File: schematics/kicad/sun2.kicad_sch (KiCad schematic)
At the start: 0 parts

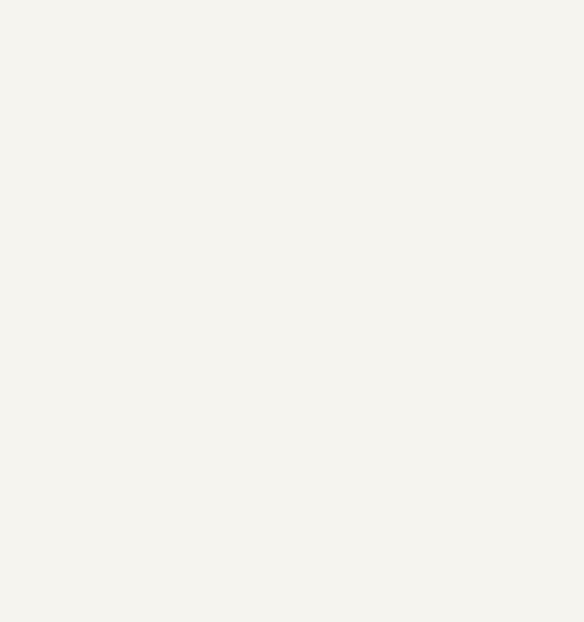
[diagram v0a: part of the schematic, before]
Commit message: System clock generator
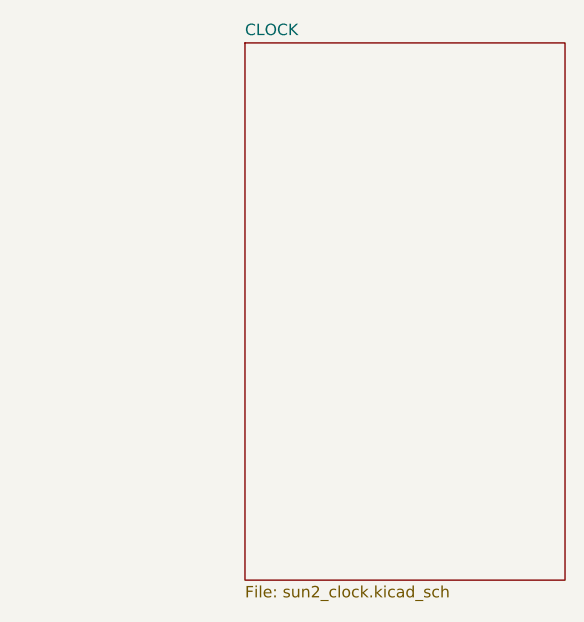
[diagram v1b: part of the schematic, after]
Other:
- added sheet CLOCK (sun2_clock.kicad_sch)
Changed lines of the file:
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@@
+		)
+	)
+	(sheet
+		(at 100.33 35.56)
+		(size 35.56 59.69)
+		(exclude_from_sim no)
+		(in_bom yes)
+		(on_board yes)
+		(dnp no)
+		(fields_autoplaced yes)
+		(stroke
+			(width 0.1524)
+			(type solid)
+		)
+		(fill
+			(color 0 0 0 0.0000)
+		)
+		(property "Sheetname" "CLOCK"
+			(at 100.33 34.8484 0)
+			(effects
+				(font
+					(size 1.27 1.27)
+				)
+				(justify left bottom)
+			)
+		)
+		(property "Sheetfile" "sun2_clock.kicad_sch"
+			(at 100.33 95.8346 0)
+			(effects
+				(font
+					(size 1.27 1.27)
+				)
+				(justify left top)
+			)
+		)
+		(instances
+			(project "sun2"
+				(path "/67ee2072-0b57-4a50-8537-b17b5f651e89"
+					(page "3")
+				)
+			)
 		)
 	)

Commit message: more mmu work
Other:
- added sheet MMU (sun2_mmu.kicad_sch)
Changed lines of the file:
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@@
+		)
+	)
+	(sheet
+		(at 151.13 35.56)
+		(size 36.83 59.69)
+		(exclude_from_sim no)
+		(in_bom yes)
+		(on_board yes)
+		(dnp no)
+		(fields_autoplaced yes)
+		(stroke
+			(width 0.1524)
+			(type solid)
+		)
+		(fill
+			(color 0 0 0 0.0000)
+		)
+		(property "Sheetname" "MMU"
+			(at 151.13 34.8484 0)
+			(effects
+				(font
+					(size 1.27 1.27)
+				)
+				(justify left bottom)
+			)
+		)
+		(property "Sheetfile" "sun2_mmu.kicad_sch"
+			(at 151.13 95.8346 0)
+			(effects
+				(font
+					(size 1.27 1.27)
+				)
+				(justify left top)
+			)
+		)
+		(instances
+			(project "sun2"
+				(path "/67ee2072-0b57-4a50-8537-b17b5f651e89"
+					(page "4")
+				)
+			)
 		)
 	)

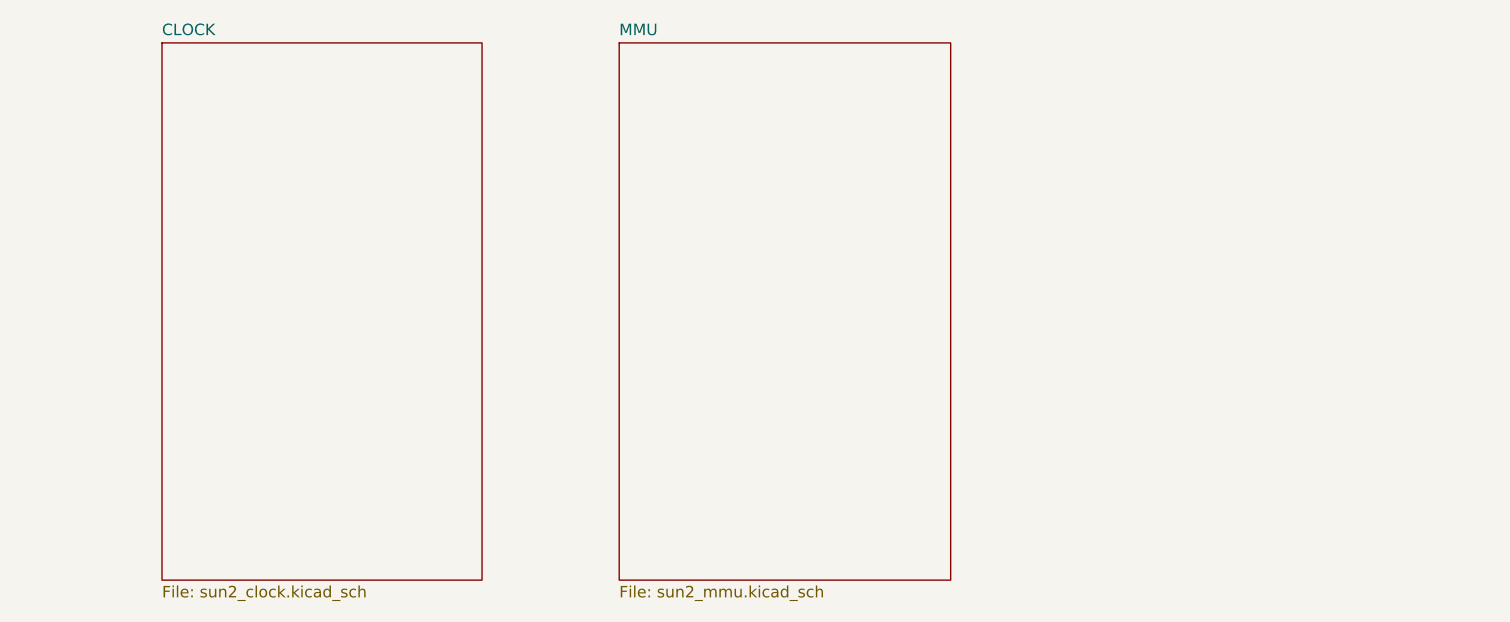
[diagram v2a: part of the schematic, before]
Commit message: PROM, RTC, Registers work
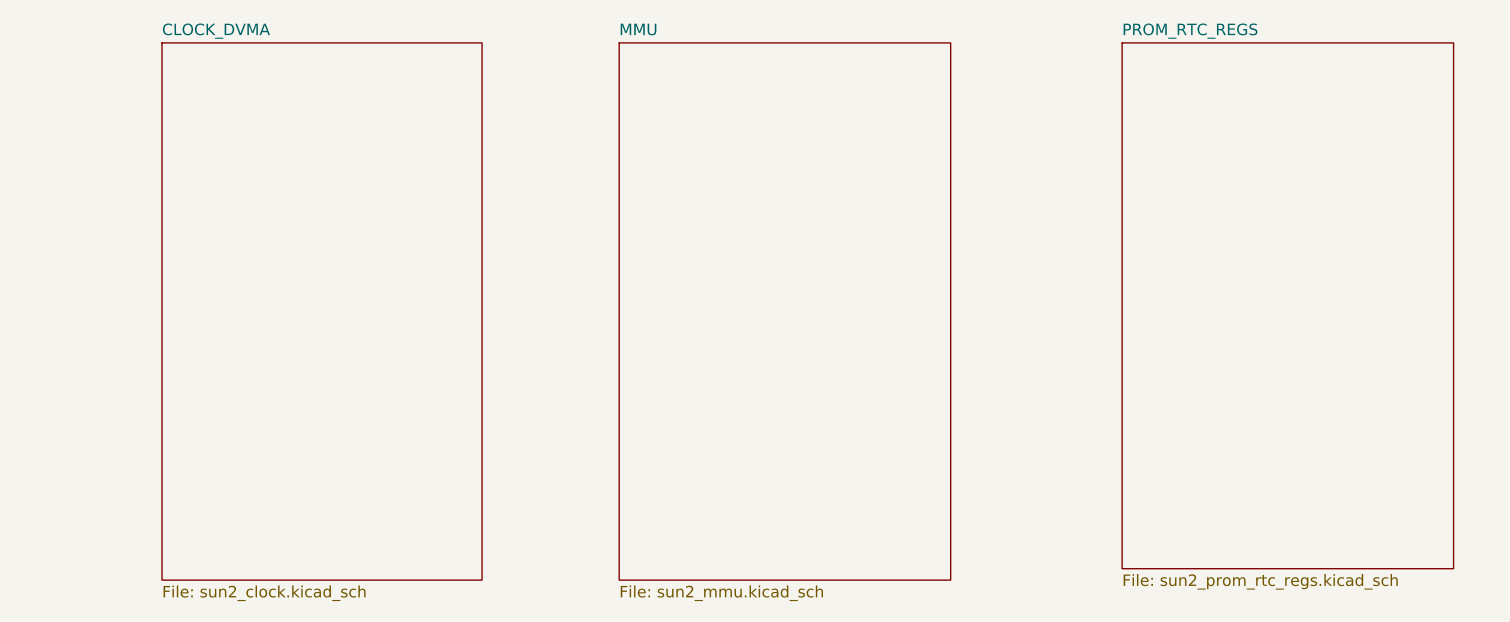
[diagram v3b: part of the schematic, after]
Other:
- sheet CLOCK renamed CLOCK_DVMA
- added sheet PROM_RTC_REGS (sun2_prom_rtc_regs.kicad_sch)
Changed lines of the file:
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@@
 			(color 0 0 0 0.0000)
 		)
-		(property "Sheetname" "CLOCK"
+		(property "Sheetname" "CLOCK_DVMA"
 			(at 100.33 34.8484 0)
 			(effects
@@
 				)
 			)
+		)
+	)
+	(sheet
+		(at 207.01 35.56)
+		(size 36.83 58.42)
+		(exclude_from_sim no)
+		(in_bom yes)
+		(on_board yes)
+		(dnp no)
+		(fields_autoplaced yes)
+		(stroke
+			(width 0.1524)
+			(type solid)
+		)
+		(fill
+			(color 0 0 0 0.0000)
+		)
+		(property "Sheetname" "PROM_RTC_REGS"
+			(at 207.01 34.8484 0)
+			(effects
+				(font
+					(size 1.27 1.27)
+				)
+				(justify left bottom)
+			)
+		)
+		(property "Sheetfile" "sun2_prom_rtc_regs.kicad_sch"
+			(at 207.01 94.5646 0)
+			(effects
+				(font
+					(size 1.27 1.27)
+				)
+				(justify left top)
+			)
+		)
+		(instances
+			(project "sun2"
+				(path "/67ee2072-0b57-4a50-8537-b17b5f651e89"
+					(page "5")
+				)
+			)

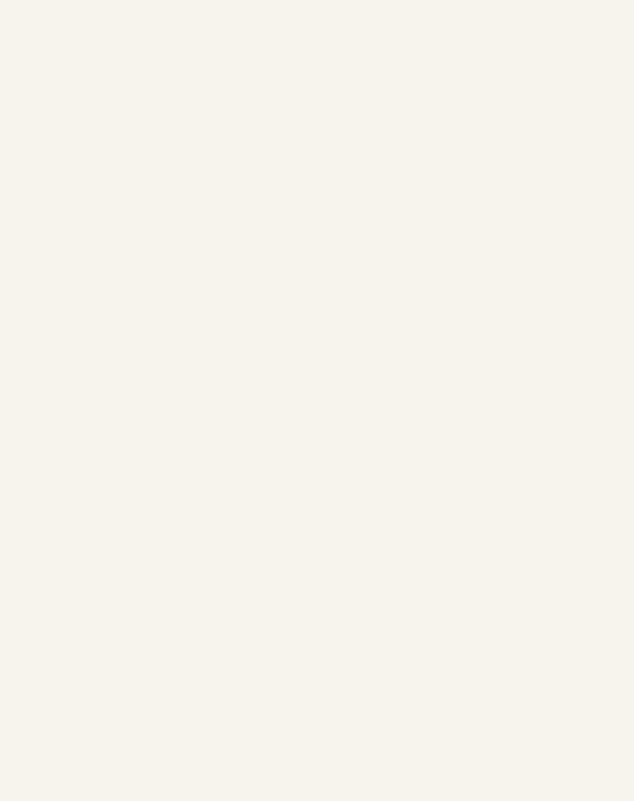
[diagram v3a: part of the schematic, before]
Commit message: Start on rasterop, parity, P2
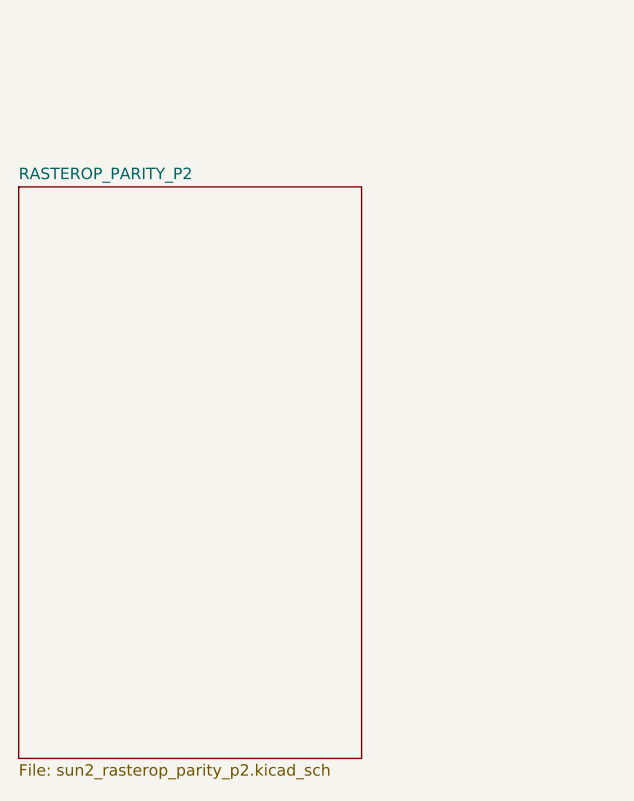
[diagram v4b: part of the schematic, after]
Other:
- added sheet RASTEROP_PARITY_P2 (sun2_rasterop_parity_p2.kicad_sch)
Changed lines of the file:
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@@
+	)
+	(sheet
+		(at 34.29 123.19)
+		(size 38.1 63.5)
+		(exclude_from_sim no)
+		(in_bom yes)
+		(on_board yes)
+		(dnp no)
+		(fields_autoplaced yes)
+		(stroke
+			(width 0.1524)
+			(type solid)
+		)
+		(fill
+			(color 0 0 0 0.0000)
+		)
+		(property "Sheetname" "RASTEROP_PARITY_P2"
+			(at 34.29 122.4784 0)
+			(effects
+				(font
+					(size 1.27 1.27)
+				)
+				(justify left bottom)
+			)
+		)
+		(property "Sheetfile" "sun2_rasterop_parity_p2.kicad_sch"
+			(at 34.29 187.2746 0)
+			(effects
+				(font
+					(size 1.27 1.27)
+				)
+				(justify left top)
+			)
+		)
+		(instances
+			(project "sun2"
+				(path "/67ee2072-0b57-4a50-8537-b17b5f651e89"
+					(page "6")
+				)
+			)
+		)
 	)
 	(sheet

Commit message: Rasterop, parity, P2 work
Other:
- added sheet PERIPHERALS (sun2_periph.kicad_sch)
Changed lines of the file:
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@@
+	)
+	(sheet
+		(at 100.33 123.19)
+		(size 35.56 63.5)
+		(exclude_from_sim no)
+		(in_bom yes)
+		(on_board yes)
+		(dnp no)
+		(fields_autoplaced yes)
+		(stroke
+			(width 0.1524)
+			(type solid)
+		)
+		(fill
+			(color 0 0 0 0.0000)
+		)
+		(property "Sheetname" "PERIPHERALS"
+			(at 100.33 122.4784 0)
+			(effects
+				(font
+					(size 1.27 1.27)
+				)
+				(justify left bottom)
+			)
+		)
+		(property "Sheetfile" "sun2_periph.kicad_sch"
+			(at 100.33 187.2746 0)
+			(effects
+				(font
+					(size 1.27 1.27)
+				)
+				(justify left top)
+			)
+		)
+		(instances
+			(project "sun2"
+				(path "/67ee2072-0b57-4a50-8537-b17b5f651e89"
+					(page "7")
+				)
+			)
+		)
 	)
 	(sheet

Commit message: 80287 and finish peripherals, start on addresses and buffers
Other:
- added sheet ADDRS_BUFFERS (sun2_addrs_buffers.kicad_sch)
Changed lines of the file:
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@@
+	)
+	(sheet
+		(at 152.4 123.19)
+		(size 31.75 59.69)
+		(exclude_from_sim no)
+		(in_bom yes)
+		(on_board yes)
+		(dnp no)
+		(fields_autoplaced yes)
+		(stroke
+			(width 0.1524)
+			(type solid)
+		)
+		(fill
+			(color 0 0 0 0.0000)
+		)
+		(property "Sheetname" "ADDRS_BUFFERS"
+			(at 152.4 122.4784 0)
+			(effects
+				(font
+					(size 1.27 1.27)
+				)
+				(justify left bottom)
+			)
+		)
+		(property "Sheetfile" "sun2_addrs_buffers.kicad_sch"
+			(at 152.4 183.4646 0)
+			(effects
+				(font
+					(size 1.27 1.27)
+				)
+				(justify left top)
+			)
+		)
+		(instances
+			(project "sun2"
+				(path "/67ee2072-0b57-4a50-8537-b17b5f651e89"
+					(page "8")
+				)
+			)
+		)
 	)
 	(sheet

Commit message: start conn
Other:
- added sheet CONNECTORS (sun2_connectors.kicad_sch)
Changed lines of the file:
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@@
 	(paper "USLetter")
+	(sheet
+		(at 207.01 123.19)
+		(size 36.83 59.69)
+		(exclude_from_sim no)
+		(in_bom yes)
+		(on_board yes)
+		(dnp no)
+		(fields_autoplaced yes)
+		(stroke
+			(width 0.1524)
+			(type solid)
+		)
+		(fill
+			(color 0 0 0 0.0000)
+		)
+		(property "Sheetname" "CONNECTORS"
+			(at 207.01 122.4784 0)
+			(effects
+				(font
+					(size 1.27 1.27)
+				)
+				(justify left bottom)
+			)
+		)
+		(property "Sheetfile" "sun2_connectors.kicad_sch"
+			(at 207.01 183.4646 0)
+			(effects
+				(font
+					(size 1.27 1.27)
+				)
+				(justify left top)
+			)
+		)
+		(instances
+			(project "sun2"
+				(path "/67ee2072-0b57-4a50-8537-b17b5f651e89"
+					(page "9")
+				)
+			)
+		)
+	)
 	(sheet
 		(at 34.29 35.56)

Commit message: Finish passives
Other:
- added sheet PASSIVES (sun2_passive.kicad_sch)
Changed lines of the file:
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@@
+	)
+	(sheet
+		(at 246.38 101.6)
+		(size 17.78 13.97)
+		(exclude_from_sim no)
+		(in_bom yes)
+		(on_board yes)
+		(dnp no)
+		(fields_autoplaced yes)
+		(stroke
+			(width 0.1524)
+			(type solid)
+		)
+		(fill
+			(color 0 0 0 0.0000)
+		)
+		(property "Sheetname" "PASSIVES"
+			(at 246.38 100.8884 0)
+			(effects
+				(font
+					(size 1.27 1.27)
+				)
+				(justify left bottom)
+			)
+		)
+		(property "Sheetfile" "sun2_passive.kicad_sch"
+			(at 246.38 116.1546 0)
+			(effects
+				(font
+					(size 1.27 1.27)
+				)
+				(justify left top)
+			)
+		)
+		(instances
+			(project "sun2"
+				(path "/67ee2072-0b57-4a50-8537-b17b5f651e89"
+					(page "10")
+				)
+			)
+		)
 	)
 	(sheet
